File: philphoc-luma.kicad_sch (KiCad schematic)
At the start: 49 parts, among them J1 SWD, J10 M3, J2 E75_proc, J3 USB_C, J4 OUT, J5 IN, J6 I2C, J7 M3, J8 M3, J9 M3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

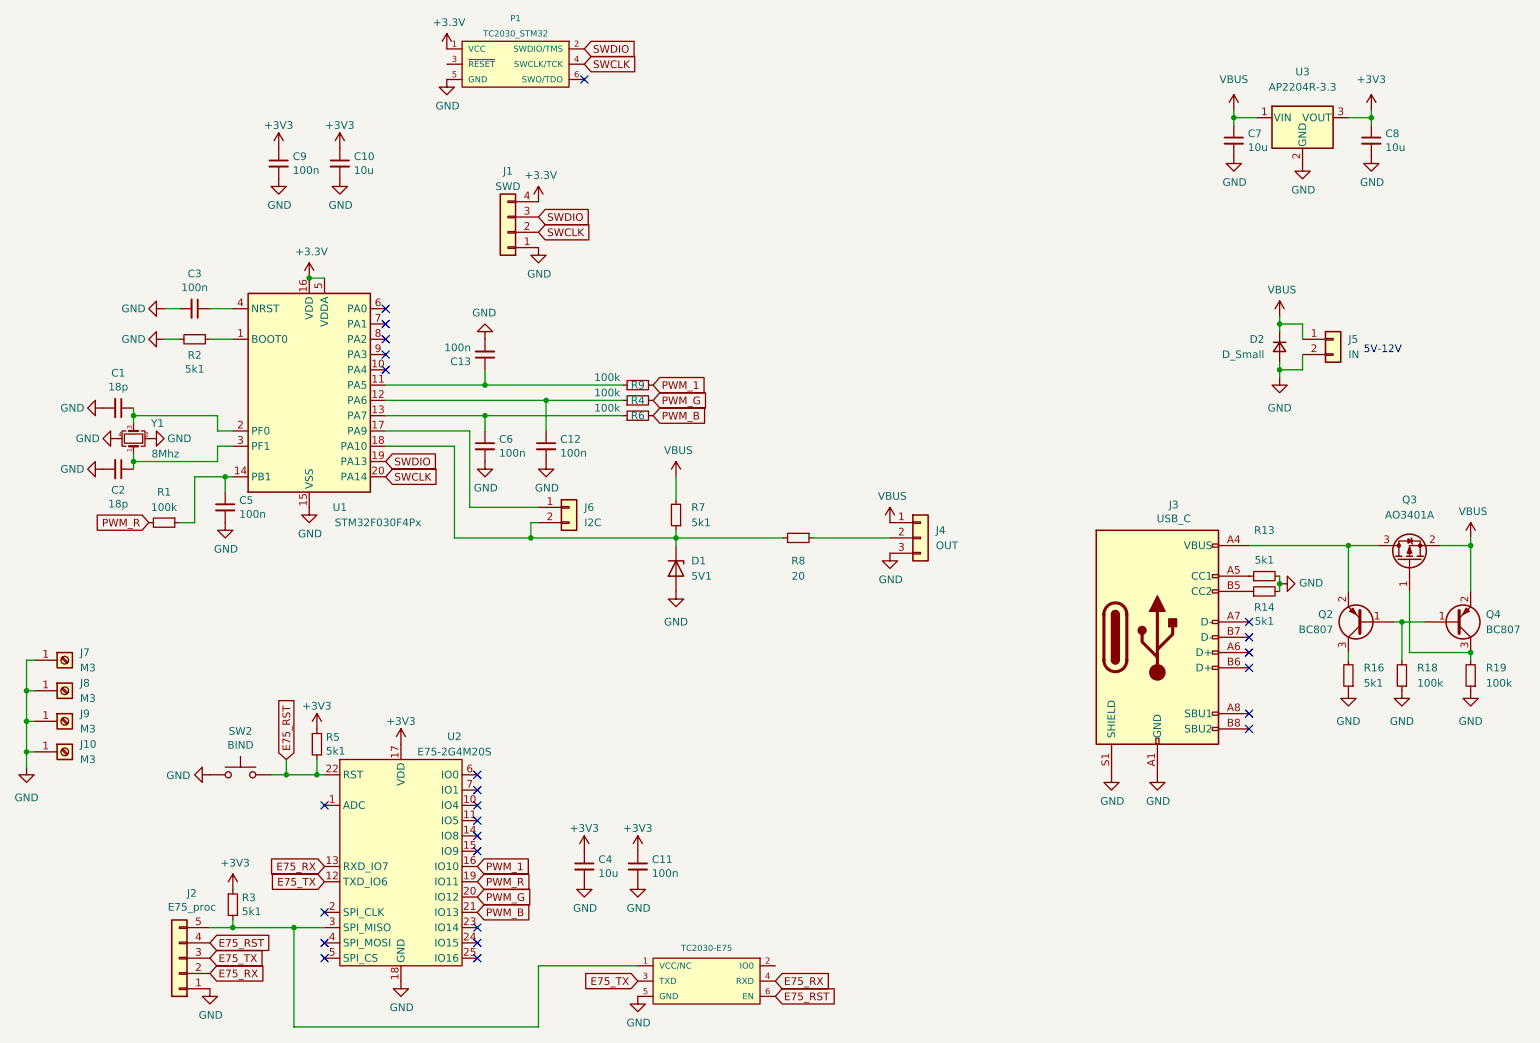
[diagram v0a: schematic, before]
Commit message: exchanged STM32f030 for STM32G030
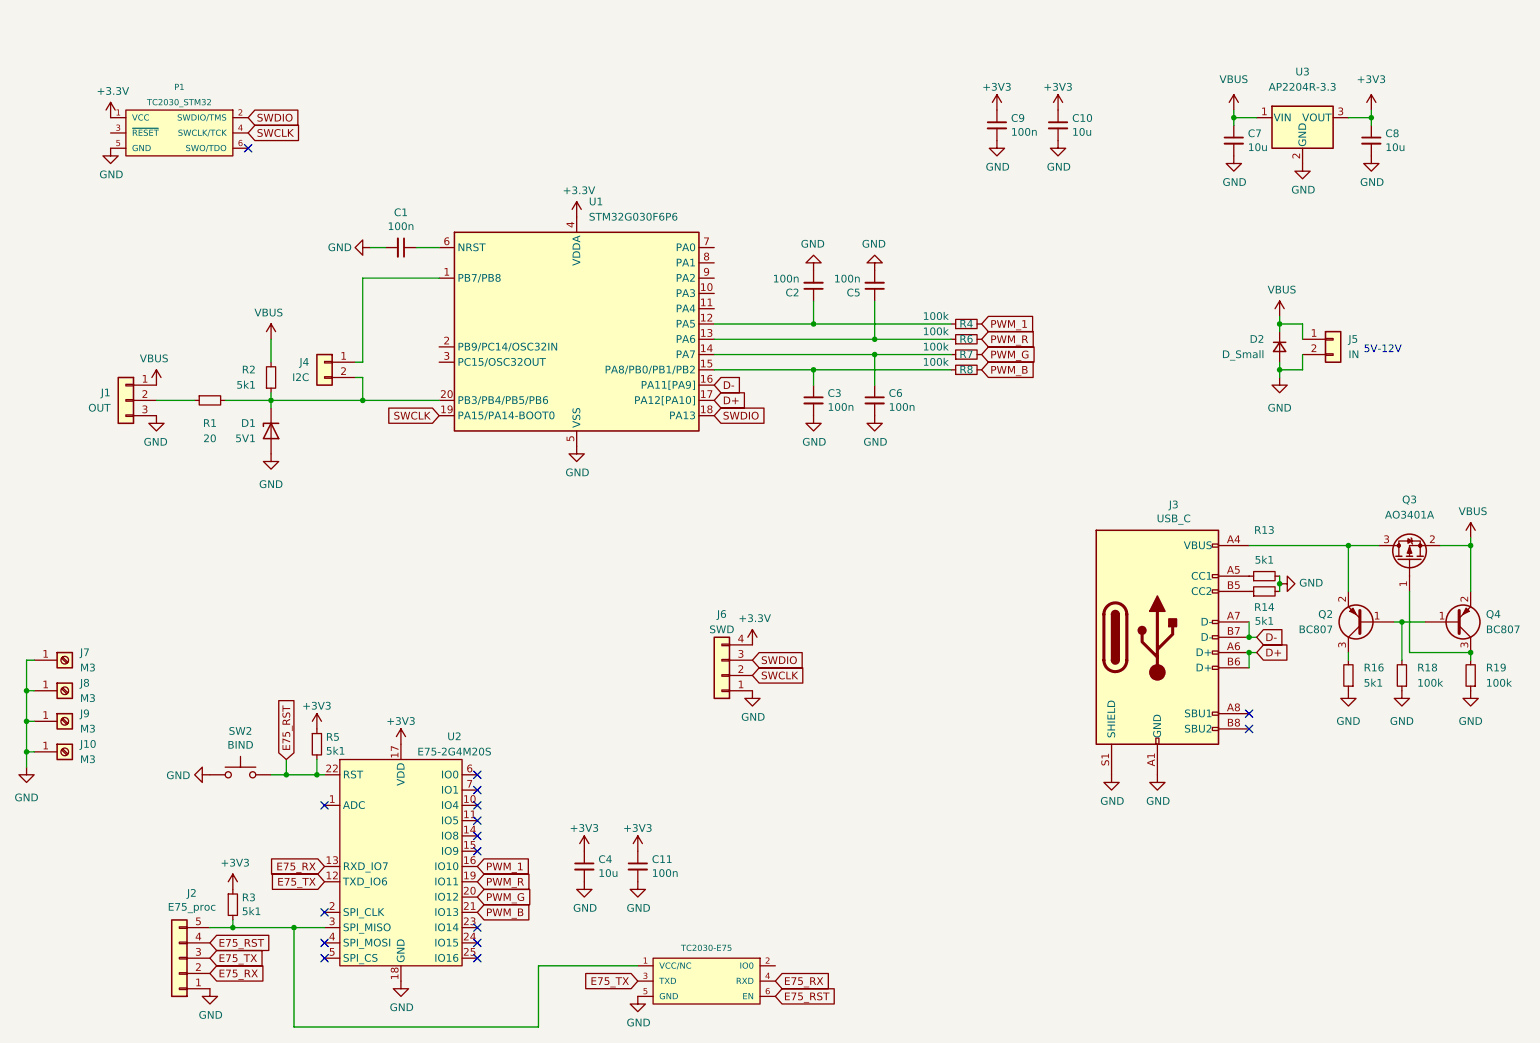
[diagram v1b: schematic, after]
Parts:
- removed C12, C13: 100n, otter:C_0402, symbol Device:C_Small
- removed J1: SWD, otter:PinSocket_1x04_P2.54mm_Vertical_center, symbol Connector_Generic:Conn_01x04
- removed J4: OUT, Connector_Phoenix_MSTB:PhoenixContact_MSTBA_2,5_3-G-5,08_1x03_P5.08mm_Horizontal, symbol Connector_Generic:Conn_01x03
- removed J6: I2C, otter:PinHeader_1x02_P2.54mm_Vertical, symbol Connector_Generic:Conn_01x02
- removed R9: 100k, otter:R_0402, symbol Device:R_Small
- removed U1: STM32F030F4Px, Package_SO:TSSOP-20_4.4x6.5mm_P0.65mm, symbol MCU_ST_STM32F0:STM32F030F4Px
- removed Y1: 8Mhz, otter:Oscillator_3225, symbol Device:Crystal_GND24_Small
- added J1: OUT, Connector_Phoenix_MSTB:PhoenixContact_MSTBA_2,5_3-G-5,08_1x03_P5.08mm_Horizontal, symbol Connector_Generic:Conn_01x03
- added J4: I2C, otter:PinHeader_1x02_P2.54mm_Vertical, symbol Connector_Generic:Conn_01x02
- added J6: SWD, otter:PinSocket_1x04_P2.54mm_Vertical_center, symbol Connector_Generic:Conn_01x04
- added U1: STM32G030F6P6, Package_SO:TSSOP-20_4.4x6.5mm_P0.65mm, symbol otter:STM32G030F6P6
- C1, C2: value 18p -> 100n
- R1: value 100k -> 20
- R7: value 5k1 -> 100k
- R8: value 20 -> 100k
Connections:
- net +3V3: now also J6.4 (Pin_4), U1.4 (VDDA)
- net GND: now also J1.3 (Pin_3), J6.1 (Pin_1), U1.5 (VSS); no longer R2.2
- net PWM_1: now also R4.2
- net PWM_B: now also R8.2; no longer R6.2
- net PWM_G: now also R7.2; no longer R4.2
- net PWM_R: now also R6.2; no longer R1.2
- net SWCLK: now also J6.2 (Pin_2), U1.19 (PA15/PA14-BOOT0)
- net SWDIO: now also J6.3 (Pin_3), U1.18 (PA13)
- net VBUS: now also R2.2, J1.1 (Pin_1); no longer R7.2
- net D+: now reaches J3.A6 (D+)
- net D+: now also J3.B6 (D+), U1.17 (PA12[PA10])
- net D-: now reaches J3.A7 (D-)
- net D-: now also J3.B7 (D-), U1.16 (PA11[PA9])
- net at R6.1: now also C5.1, U1.13 (PA6); no longer C6.1
- net at C3.1: now also R8.1, U1.15 (PA8/PB0/PB1/PB2)
- net at R2.1: now also D1.1 (K), R1.2, J4.2 (Pin_2), U1.20 (PB3/PB4/PB5/PB6)
- net at R4.1: now also C2.1, U1.12 (PA5)
- net at R1.1: now also J1.2 (Pin_2); no longer C5.1
- net at C1.1: now also U1.6 (NRST)
- new net: J4.1 (Pin_1), U1.1 (PB7/PB8)
- new net: C6.1, R7.1, U1.14 (PA7)
- no-connect marks 25 -> 16
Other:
- moved on the sheet: C10, C9, P1

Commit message: updated sch
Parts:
- R2: value 5k1 -> 200
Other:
- note added: "Optional"
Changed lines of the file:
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@@
     (stroke (width 0) (type default) (color 0 0 0 0))
+  )
+  (text "Optional" (at 64.77 93.98 0)
+    (effects (font (size 1.27 1.27)) (justify left bottom))
   )
   (text "5V-12V\n" (at 243.84 80.01 0)
@@
       (effects (font (size 1.27 1.27)) (justify right))
     )
-    (property "Value" "5k1" (id 1) (at 59.69 85.0899 0)
+    (property "Value" "200" (id 1) (at 59.69 85.0899 0)
       (effects (font (size 1.27 1.27)) (justify right))
     )
@@
     )
     (path "/4335c9f2-6efb-4b5c-8474-bc3351b7a55c"
-      (reference "R2") (unit 1) (value "5k1") (footprint "otter:R_0402")
+      (reference "R2") (unit 1) (value "200") (footprint "otter:R_0402")
     )
     (path "/00000000-0000-0000-0000-000061cb9bfe"
